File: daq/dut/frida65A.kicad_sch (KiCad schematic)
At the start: 100 parts, among them J1 SMA Molex 733910070, J2 SMA Molex 733910070, J3 SMA Molex 733910070, J4 RJ45 Molex 446200002, J5 DisplayPort Molex 472720024, J6 MiniFitJr Molex 469990014, J7 Conn_02x06_Odd_Even, Q1 NMOS, U1 ASIC FRIDA 65A, U2 LevelShifter TI TXV0106Q1, U3 DiffAmp TI THS4541

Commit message: Updated pcb layout, added some todo
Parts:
- C1, C10, C11, C12, C13, C14, C15, C16, C17, C18, C19, C2, C20, C21, C22, C23, C24, C25, C26, C27, C28, C29, C3, C30, C31, C32, C4, C5, C6, C7, C8, C9: footprint Capacitor_SMD:C_0603_1608Metric -> Capacitor_SMD:C_0402_1005Metric
- FB1, FB2, FB3, R1, R10, R11, R12, R13, R14, R15, R16, R17, R18, R19, R2, R20, R21, R22, R23, R24, R25, R3, R4, R5, R6, R7, R8, R9, TH1: footprint Resistor_SMD:R_0603_1608Metric -> Resistor_SMD:R_0402_1005Metric
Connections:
- net GND: now also J1.2 (Ext), J2.2 (Ext), J3.2 (Ext); no longer J1.1 (In), J2.1 (In), J3.1 (In)
- net VDD_DAC: now also R20.2
- net VDD_IO: no longer C31.1, C32.1, R20.2
- net VIN_N_EXT: now also J2.1 (In); no longer J2.2 (Ext)
- net VIN_P_EXT: now also J1.1 (In); no longer J1.2 (Ext)
- net VOCM_EXT: now also C31.1, C32.1, J3.1 (In); no longer J3.2 (Ext)
- net at R19.1, R22.2, U3.4 (IN+): no longer D1.3 (K)
- net at R18.1, R23.2, U3.6 (IN-): no longer D2.3 (K)
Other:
- moved on the sheet: D1, D2, J1, J2, J3, R16

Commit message: Leaf device generation, docs on layout proto, rules/dimension proto, and constraints proto
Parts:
- added C33, C34: 51pF, Capacitor_SMD:C_0402_1005Metric, symbol Device:C
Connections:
- net CLK_COMP_N: now also J5.3, R1.2, R6.1; no longer J5.4, R2.1, R7.1
- net CLK_COMP_P: now also J5.1, R1.1, R5.1; no longer J5.6, R2.2, R8.1
- net CLK_INIT_N: now also J5.15; no longer J5.10
- net CLK_INIT_P: now also J5.17; no longer J5.12
- net CLK_LOGIC_N: now also J5.6, R2.2, R8.1; no longer J5.1, R1.1, R5.1
- net CLK_LOGIC_P: now also J5.4, R2.1, R7.1; no longer J5.3, R1.2, R6.1
- net CLK_SAMP_N: now also J5.10; no longer J5.7
- net CLK_SAMP_P: now also J5.12; no longer J5.9
- net COMP_OUT_N: now also J5.7; no longer J5.17
- net COMP_OUT_P: now also J5.9; no longer J5.15
- net VDD_DAC: now also D1.2 (A), D2.2 (A)
- net VDD_DAQ: no longer J4.7
- net VDD_IO: no longer D1.2 (A), D2.2 (A)
- net at R22.1, R24.2, U3.1 (OUT-): now also C34.2
- net at R19.1, R22.2, U3.4 (IN+): now also C34.1
- net at R18.1, R23.2, U3.6 (IN-): now also C33.1
- net at R23.1, R25.2, U3.9 (OUT+): now also C33.2
- net VDD_BDAQ: now reaches J4.8
- net VDD_BDAQ: now also J4.7
- no-connect marks 5 -> 4
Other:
- moved on the sheet: R10, R11, R12, R3, R4, R5, R6, R7, R8, R9, TH1

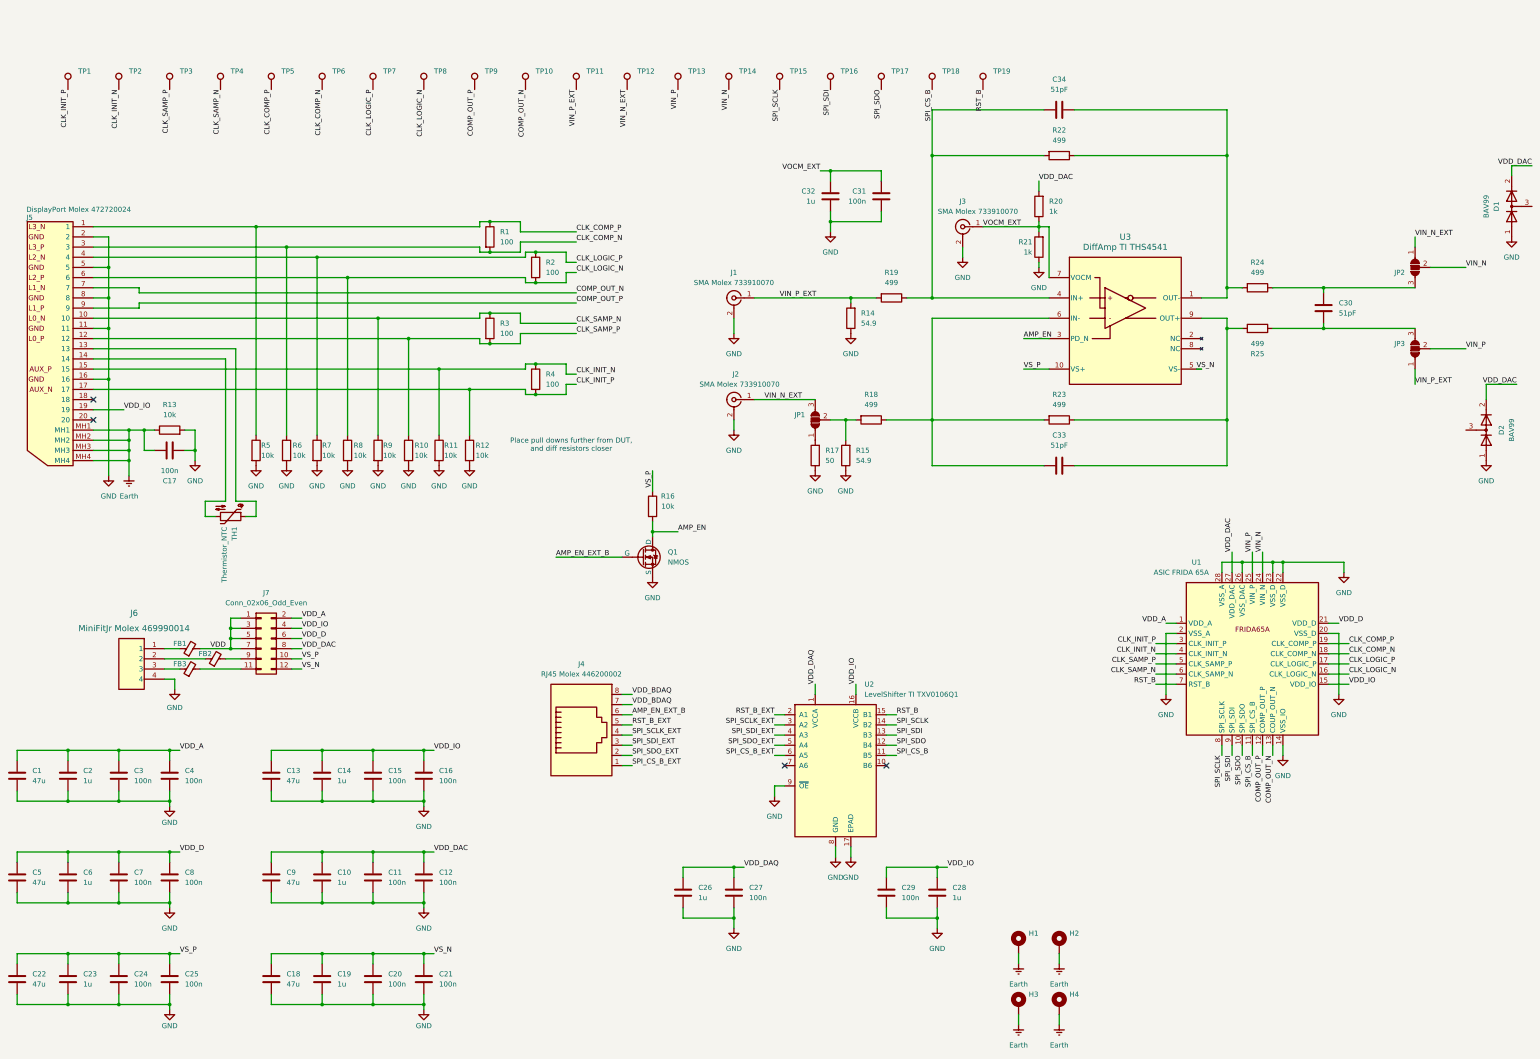
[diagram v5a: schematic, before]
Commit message: Add pcb decal
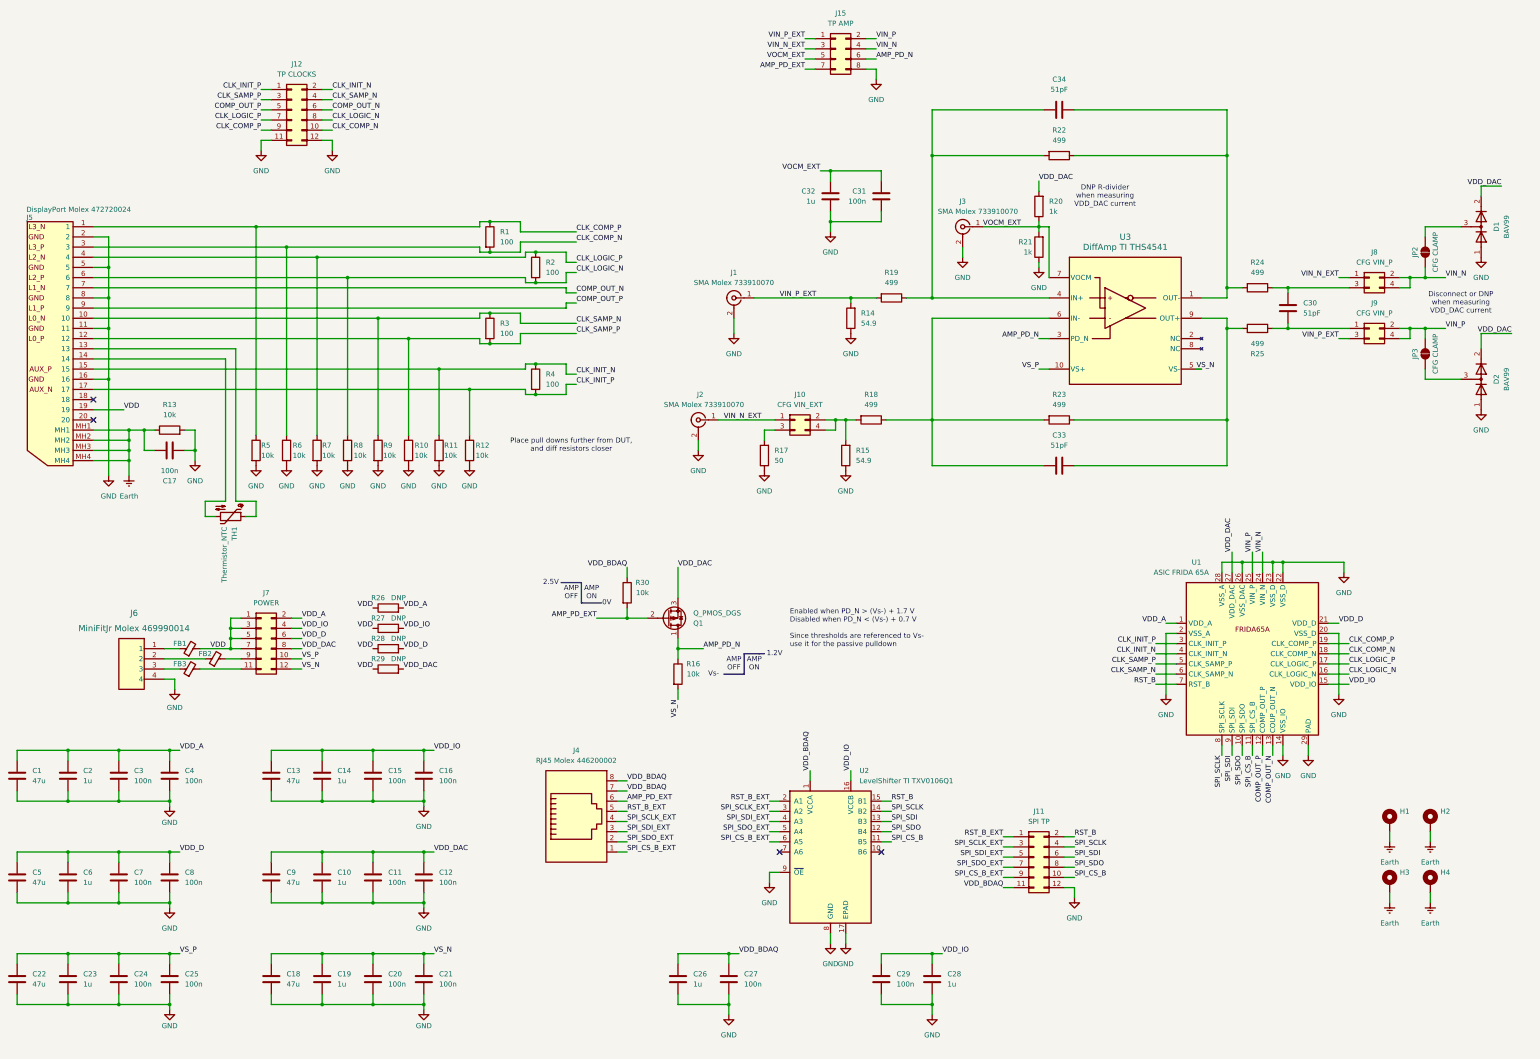
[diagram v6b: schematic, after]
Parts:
- removed JP1, JP2, JP3: SolderJumper_3_Open, Jumper:SolderJumper-3_P1.3mm_Open_RoundedPad1.0x1.5mm_NumberLabels, symbol Jumper:SolderJumper_3_Open
- removed Q1: NMOS, Package_TO_SOT_SMD:SOT-23, symbol Simulation_SPICE:NMOS
- removed TP1, TP10, TP2, TP3, TP4, TP5, TP6, TP7, TP8, TP9: TestPoint Keystone 5001, frida:Test_Point, symbol Connector:TestPoint
- removed TP11, TP12, TP13, TP14, TP15, TP16, TP17, TP18, TP19: TestPoint, TestPoint:TestPoint_Pad_D2.0mm, symbol Connector:TestPoint
- added J10: CFG VIN_EXT, Connector_PinHeader_2.54mm:PinHeader_2x02_P2.54mm_Vertical, symbol Connector_Generic:Conn_02x02_Odd_Even
- added J11: SPI TP, Connector_PinHeader_2.54mm:PinHeader_2x06_P2.54mm_Vertical, symbol Connector_Generic:Conn_02x06_Odd_Even
- added J12: TP CLOCKS, Connector_PinHeader_2.54mm:PinHeader_2x06_P2.54mm_Vertical, symbol Connector_Generic:Conn_02x06_Odd_Even
- added J15: TP AMP, Connector_PinHeader_2.54mm:PinHeader_2x04_P2.54mm_Vertical, symbol Connector_Generic:Conn_02x04_Odd_Even
- added J8, J9: CFG VIN_P, Connector_PinHeader_2.54mm:PinHeader_2x02_P2.54mm_Vertical, symbol Connector_Generic:Conn_02x02_Odd_Even
- added JP2, JP3: CFG CLAMP, Jumper:SolderJumper-2_P1.3mm_Open_RoundedPad1.0x1.5mm, symbol Jumper:SolderJumper_2_Open
- added Q1: Q_PMOS_DGS, symbol Transistor_FET:Q_PMOS_DGS
- added R26, R27, R28, R29: DNP, symbol Device:R
- added R30: 10k, Resistor_SMD:R_0402_1005Metric, symbol Device:R
- J7: value Conn_02x06_Odd_Even -> POWER
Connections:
- net VDD_DAQ is gone; now on net VDD_BDAQ: C26.1, C27.1, U2.1 (VCCA)
- net CLK_COMP_N: now also J12.10 (Pin_10)
- net CLK_COMP_P: now also J12.9 (Pin_9)
- net CLK_INIT_N: now also J12.2 (Pin_2)
- net CLK_INIT_P: now also J12.1 (Pin_1)
- net CLK_LOGIC_N: now also J12.8 (Pin_8)
- net CLK_LOGIC_P: now also J12.7 (Pin_7)
- net CLK_SAMP_N: now also J12.4 (Pin_4)
- net CLK_SAMP_P: now also J12.3 (Pin_3)
- net COMP_OUT_N: now also J12.6 (Pin_6)
- net COMP_OUT_P: now also J12.5 (Pin_5)
- net GND: now also U1.29 (PAD), J11.12 (Pin_12), J12.11 (Pin_11), J12.12 (Pin_12), J15.8 (Pin_8)
- net RST_B: now also J11.2 (Pin_2)
- net RST_B_EXT: now also J11.1 (Pin_1)
- net SPI_CS_B: now also J11.10 (Pin_10)
- net SPI_CS_B_EXT: now also J11.9 (Pin_9)
- net SPI_SCLK: now also J11.4 (Pin_4)
- net SPI_SCLK_EXT: now also J11.3 (Pin_3)
- net SPI_SDI: now also J11.6 (Pin_6)
- net SPI_SDI_EXT: now also J11.5 (Pin_5)
- net SPI_SDO: now also J11.8 (Pin_8)
- net SPI_SDO_EXT: now also J11.7 (Pin_7)
- net VDD: now also J5.19, R26.1, R27.1, R28.1, R29.1
- net VDD_A: now also R26.2
- net VDD_BDAQ: now also J11.11 (Pin_11), R30.1
- net VDD_D: now also R28.2
- net VDD_DAC: now also Q1.3 (S), R29.2
- net VDD_IO: now also R27.2; no longer J5.19
- net VIN_N: now also J15.4 (Pin_4), J8.2 (Pin_2), J8.4 (Pin_4), JP2.2 (B)
- net VIN_N_EXT: now also J10.1 (Pin_1), J15.3 (Pin_3), J8.1 (Pin_1)
- net VIN_P: now also J15.2 (Pin_2), J9.2 (Pin_2), J9.4 (Pin_4), JP3.1 (A)
- net VIN_P_EXT: now also J15.1 (Pin_1), J9.3 (Pin_3)
- net VOCM_EXT: now also J15.5 (Pin_5)
- net VS_N: now also R16.2
- net VS_P: no longer R16.1
- net at D1.3 (K): now also JP2.1 (A)
- net at R15.2, R18.2: now also J10.2 (Pin_2), J10.4 (Pin_4)
- net at R17.2: now also J10.3 (Pin_3)
- net at C30.1, R24.1: now also J8.3 (Pin_3)
- net at C30.2, R25.1: now also J9.1 (Pin_1)
- net at D2.3 (K): now also JP3.2 (B)
- net AMP_EN renamed AMP_PD_N
- net AMP_PD_N: now also R16.1, J15.6 (Pin_6), Q1.1 (D); no longer R16.2
- net AMP_EN_EXT_B renamed AMP_PD_EXT
- net AMP_PD_EXT: now also J15.7 (Pin_7), Q1.2 (G), R30.2
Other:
- note added: "0V"
- note added: "1.2V"
- note added: "2.5V"
- note added: "AMP OFF"
- note added: "AMP ON"
- note added: "DNP R-divider when measuring VDD_DAC current"
- note added: "Disconnect or DNP when measuring VDD_DAC current"
- note added: "Enabled when PD_N > (Vs-) + 1.7 V Disabled when PD_N < (Vs-) + 0.7 V Since thresholds are referenced to Vs- use it for the passive pulldown"
- note added: "Vs-"
- moved on the sheet: C26, C27, C28, C29, C30, D1, D2, H1, H2, H3, H4, J2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

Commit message: Schematic TODOs complete
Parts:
- removed U2: LevelShifter TI TXV0106Q1, frida:TI_LevelShifter_TXV0106Q1, symbol frida:TI_LevelShifter_TXV0106Q1
- added R31, R32, R33, R34: 10k, Resistor_SMD:R_0402_1005Metric, symbol Device:R
- added U2: TI LevelShifter SN74AXC8T245RJWR, frida:TI_LevelShifter_SN74AXC8T245RJWR, symbol frida:TI_LevelShifter_SN74AXC8T245RJWR
- R10, R11, R12, R5, R6, R7, R8, R9: value 10k -> 1k
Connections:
- net Earth: no longer H1.1, H2.1, H3.1, H4.1
- net GND: now also J4.7, U2.11 (GND), U2.12 (GND), U2.13 (B8), U2.14 (B7), U2.15 (B6)
- net RST_B: now also R31.2, U2.20 (B1)
- net RST_B_EXT: now also U2.2 (A1)
- net SPI_CS_B: now also U2.17 (B4)
- net SPI_CS_B_EXT: now also U2.5 (A4)
- net SPI_SCLK: now also U2.19 (B2)
- net SPI_SCLK_EXT: now also U2.3 (A2)
- net SPI_SDI: now also U2.18 (B3)
- net SPI_SDI_EXT: now also U2.4 (A3)
- net SPI_SDO: now also U2.16 (B5)
- net SPI_SDO_EXT: now also U2.6 (A5)
- net VDD_BDAQ: now also Q1.3 (S), R32.1, R33.1, R34.1, U2.24 (VCCA); no longer J4.7
- net VDD_DAC: no longer Q1.3 (S)
- net VDD_IO: now also R31.1, U2.22 (VCCB), U2.23 (VCCB)
- new net: R32.2, U2.21 (OE_N)
- new net: R33.2, U2.1 (DIR1)
- new net: R34.2, U2.10 (DIR2)
- no-connect marks 4 -> 9
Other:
- note added: "Place as empty pads, on the board backside"
- moved on the sheet: C26, C27, C28, C29, H1, H2, H3, H4, J11, J4, Q1, R16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

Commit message: Add attenuator configuration to PCB
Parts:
- removed J8, J9: CFG VIN_P, Connector_PinHeader_2.54mm:PinHeader_2x02_P2.54mm_Vertical, symbol Connector_Generic:Conn_02x02_Odd_Even
- added J13: VIN CFG, Connector_PinHeader_2.54mm:PinHeader_2x04_P2.54mm_Vertical, symbol Connector_Generic:Conn_02x04_Odd_Even
- added J14: ATTEN CFG, Connector_PinHeader_2.54mm:PinHeader_2x04_P2.54mm_Vertical, symbol Connector_Generic:Conn_02x04_Odd_Even
- added R35, R36: DNP, Resistor_SMD:R_0402_1005Metric, symbol Device:R
- J10: value CFG VIN_EXT -> DIFF/SE CFG
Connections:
- net VIN_N: now also J13.2 (Pin_2), J13.4 (Pin_4)
- net VIN_N_EXT: now also J13.1 (Pin_1)
- net VIN_P: now also J13.6 (Pin_6), J13.8 (Pin_8)
- net VIN_P_EXT: now also J13.7 (Pin_7), R36.2
- net at C30.2, R25.1: now also J13.5 (Pin_5)
- net at C34.1, R22.2, U3.4 (IN+): now also J14.2 (Pin_2), J14.4 (Pin_4); no longer R19.1
- net at J10.2 (Pin_2), J10.4 (Pin_4), R15.2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: now also R35.2
- net at C33.1, R23.2, U3.6 (IN-): now also J14.6 (Pin_6), J14.8 (Pin_8); no longer R18.1
- net at C30.1, R24.1: now also J13.3 (Pin_3)
- new net: J14.1 (Pin_1), R36.1
- new net: J14.5 (Pin_5), R18.1
- new net: J14.7 (Pin_7), R35.1
- new net: J14.3 (Pin_3), R19.1
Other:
- note added: "Attenuator:"
- note added: "Buffer:"
- note added: "Bypass:"
- note added: "Diff:"
- note added: "DiffAmp:"
- note added: "RX"
- note added: "Single-Ended:"
- note added: "TX"
- moved on the sheet: C17, C26, C27, C28, C29, C30, C31, C32, C33, C34, D1, D2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
